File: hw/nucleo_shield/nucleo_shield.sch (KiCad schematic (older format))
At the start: 13 parts, among them CN101 Nucleo-F411RE-CN10, CN71 Nucleo-F411RE-CN7, P12 CONN_RS485_OUT, P13 CONN_RS485_IN, P4 POWER_CON, P6 ETH_CONN, P7 SD_CONN, P8 LCD_CONN, P9 CONN_SCT

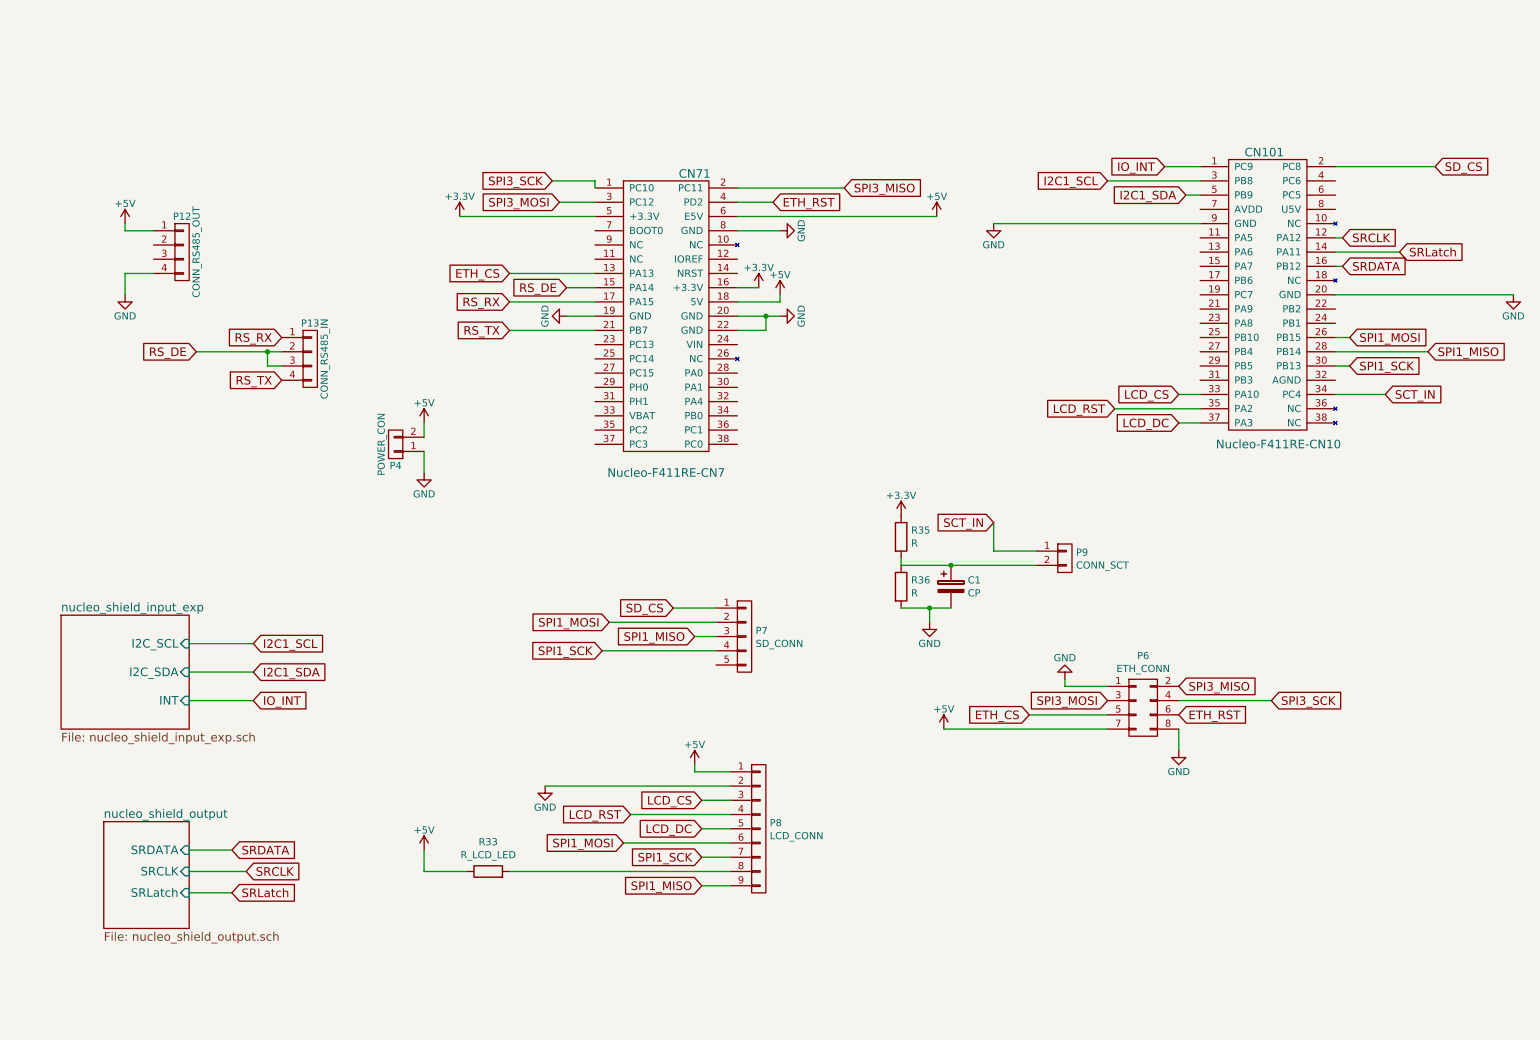
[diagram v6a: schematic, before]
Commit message: Nucleo: add jumpers and outputs
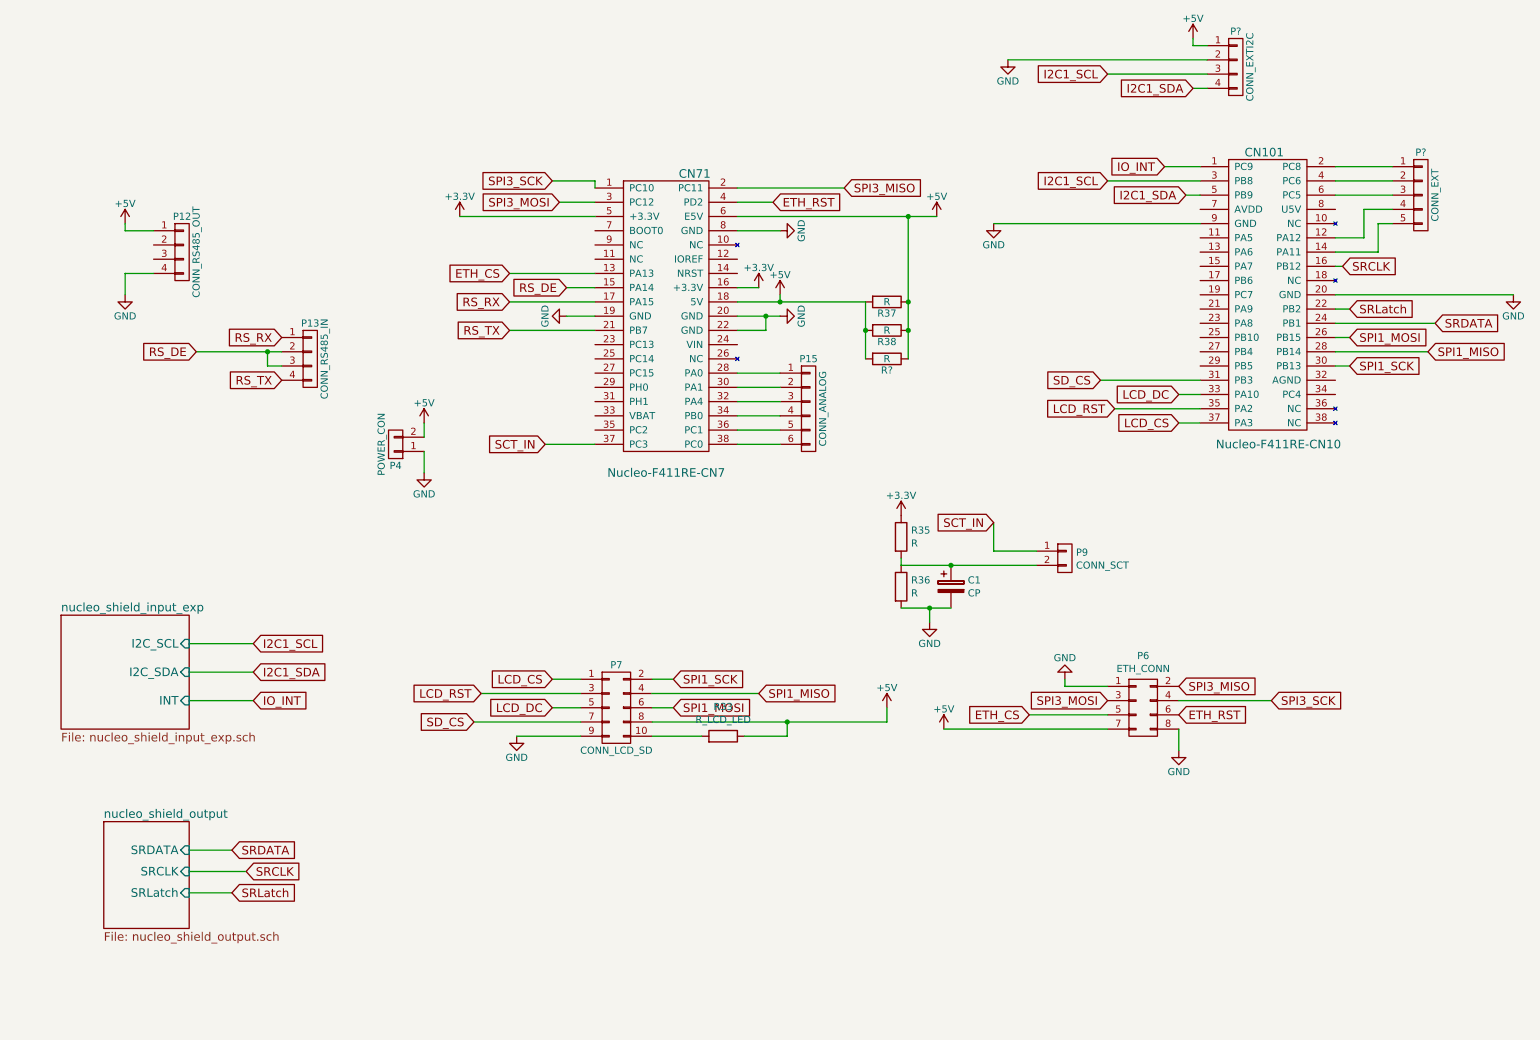
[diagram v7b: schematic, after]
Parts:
- removed P7: SD_CONN, Pin_Headers:Pin_Header_Straight_1x05, symbol CONN_01X05
- removed P8: LCD_CONN, Pin_Headers:Pin_Header_Straight_1x09, symbol CONN_01X09
- added P15: CONN_ANALOG, Pin_Headers:Pin_Header_Straight_1x06, symbol CONN_01X06
- added P7: CONN_LCD_SD, Pin_Headers:Pin_Header_Straight_2x05, symbol CONN_02X05
- added P?: CONN_EXT, symbol CONN_01X05
- added P?: CONN_EXTI2C, symbol CONN_01X04
- added R37, R38, R?: R, Resistors_ThroughHole:Resistor_Horizontal_RM10mm, symbol R
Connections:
- net +5V: now also P7.8 (P8), P?.1 (P1), R37.1, R37.2, R38.1, R38.2, R?.1, R?.2
- net GND: now also P7.9 (P9), P?.2 (P2)
- net I2C1_SCL: now also P?.3 (P3)
- net I2C1_SDA: now also P?.4 (P4)
- net LCD_CS: now also CN101.37 (PA3), P7.1 (P1); no longer CN101.33 (PA10)
- net LCD_DC: now also CN101.33 (PA10), P7.5 (P5); no longer CN101.37 (PA3)
- net LCD_RST: now also P7.3 (P3)
- net SCT_IN: now also CN71.37 (PC3); no longer CN101.34 (PC4)
- net SD_CS: now also CN101.31 (PB3), P7.7 (P7); no longer CN101.2 (PC8)
- net SPI1_MISO: now also P7.4 (P4)
- net SPI1_MOSI: now also P7.6 (P6)
- net SPI1_SCK: now also P7.2 (P2)
- net SRCLK: now also CN101.16 (PB12); no longer CN101.12 (PA12)
- net SRDATA: now also CN101.24 (PB1); no longer CN101.16 (PB12)
- net SRLatch: now also CN101.22 (PB2); no longer CN101.14 (PA11)
- net at CN101.4 (PC6): now also P?.2 (P2)
- net at CN101.6 (PC5): now also P?.3 (P3)
- net at CN71.28 (PA0): now also P15.1 (P1)
- net at CN71.30 (PA1): now also P15.2 (P2)
- net at CN71.32 (PA4): now also P15.3 (P3)
- net at CN71.34 (PB0): now also P15.4 (P4)
- net at CN71.36 (PC1): now also P15.5 (P5)
- net at CN71.38 (PC0): now also P15.6 (P6)
- net at R33.2: now also P7.10 (P10)
- new net: CN101.12 (PA12), P?.4 (P4)
- new net: CN101.14 (PA11), P?.5 (P5)
- new net: CN101.2 (PC8), P?.1 (P1)
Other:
- moved on the sheet: R33

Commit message: Add one wire, expander, etc
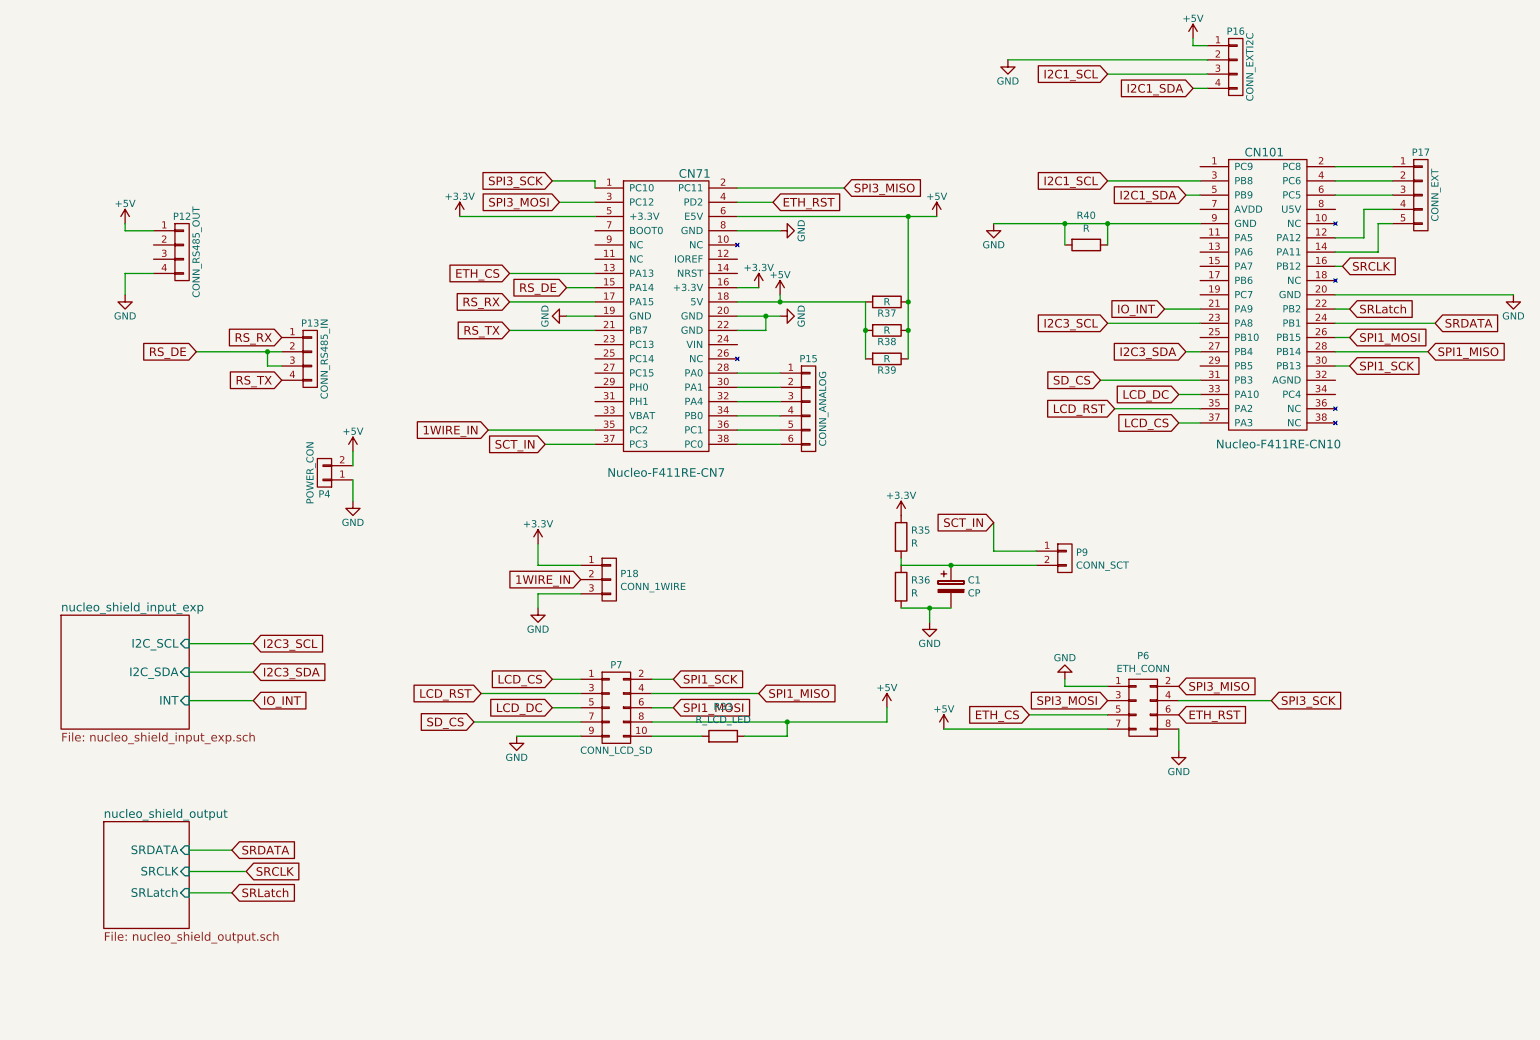
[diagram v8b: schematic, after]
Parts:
- removed R?: R, Resistors_ThroughHole:Resistor_Horizontal_RM10mm, symbol R
- added P18: CONN_1WIRE, Pin_Headers:Pin_Header_Straight_1x03, symbol CONN_01X03
- added R39: R, Resistors_ThroughHole:Resistor_Horizontal_RM20mm, symbol R
- added R40: R, Resistors_ThroughHole:Resistor_Horizontal_RM10mm, symbol R
- P16: renamed from P?; footprint (none) -> Pin_Headers:Pin_Header_Straight_1x04
- P17: renamed from P?; footprint (none) -> Pin_Headers:Pin_Header_Straight_1x05
- R35, R36: footprint Resistors_SMD:R_0805_HandSoldering -> Resistors_ThroughHole:Resistor_Horizontal_RM10mm
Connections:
- net +3V3: now also P18.1 (P1)
- net +5V: now also R39.1, R39.2
- net GND: now also P18.3 (P3), R40.1, R40.2
- net IO_INT: now also CN101.21 (PA9); no longer CN101.1 (PC9)
- net I2C3_SCL: now reaches CN101.23 (PA8)
- net I2C3_SDA: now reaches CN101.27 (PB4)
- net 1WIRE_IN: now reaches CN71.35 (PC2)
- net 1WIRE_IN: now also P18.2 (P2)
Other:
- moved on the sheet: P4
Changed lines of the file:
@@
 LIBS:memory
 LIBS:xilinx
-LIBS:special
 LIBS:microcontrollers
 LIBS:dsp
@@
 L CONN_01X02 P4
 U 1 1 56AB61A1
-P 3300 3600
-F 0 "P4" H 3300 3750 50  0000 C CNN
-F 1 "POWER_CON" V 3400 3600 50  0000 C CNN
-F 2 "w_conn_screw:mors_2p" H 3300 3600 60  0001 C CNN
-F 3 "" H 3300 3600 60  0000 C CNN
-	1    3300 3600
+P 2800 3800
+F 0 "P4" H 2800 3950 50  0000 C CNN
+F 1 "POWER_CON" V 2900 3800 50  0000 C CNN
+F 2 "w_conn_screw:mors_2p" H 2800 3800 60  0001 C CNN
+F 3 "" H 2800 3800 60  0000 C CNN
+	1    2800 3800
 	-1   0    0    1
 $EndComp
@@
 L +5V #PWR09
 U 1 1 56AB6530
-P 3500 3450
-F 0 "#PWR09" H 3500 3300 50  0001 C CNN
-F 1 "+5V" H 3500 3590 50  0000 C CNN
-F 2 "" H 3500 3450 60  0000 C CNN
-F 3 "" H 3500 3450 60  0000 C CNN
-	1    3500 3450
+P 3000 3650
+F 0 "#PWR09" H 3000 3500 50  0001 C CNN
+F 1 "+5V" H 3000 3790 50  0000 C CNN
+F 2 "" H 3000 3650 60  0000 C CNN
+F 3 "" H 3000 3650 60  0000 C CNN
+	1    3000 3650
 	1    0    0    -1
 $EndComp
@@
 L GND #PWR010
 U 1 1 56AB6589
-P 3500 3800
-F 0 "#PWR010" H 3500 3550 50  0001 C CNN
-F 1 "GND" H 3500 3650 50  0000 C CNN
-F 2 "" H 3500 3800 60  0000 C CNN
-F 3 "" H 3500 3800 60  0000 C CNN
-	1    3500 3800
+P 3000 4000
+F 0 "#PWR010" H 3000 3750 50  0001 C CNN
+F 1 "GND" H 3000 3850 50  0000 C CNN
+F 2 "" H 3000 4000 60  0000 C CNN
+F 3 "" H 3000 4000 60  0000 C CNN
+	1    3000 4000
 	1    0    0    -1
 $EndComp
@@
 Text GLabel 2150 6450 2    60   Input ~ 0
 SRDATA
-Text GLabel 8300 1750 0    60   Input ~ 0
-I2C1_SCL
-Text GLabel 8850 1850 0    60   Input ~ 0
-I2C1_SDA
+Text GLabel 8300 2750 0    60   Input ~ 0
+I2C3_SCL
+Text GLabel 8850 2950 0    60   Input ~ 0
+I2C3_SDA
 Text GLabel 6450 1800 2    60   Input ~ 0
 SPI3_MISO
@@
 Text GLabel 4400 1750 0    60   Input ~ 0
 SPI3_SCK
-Text GLabel 8700 1650 0    60   Input ~ 0
+Text GLabel 8700 2650 0    60   Input ~ 0
 IO_INT
 $Sheet
@@
 IO_INT
 Text GLabel 2300 5000 2    60   Input ~ 0
-I2C1_SCL
+I2C3_SCL
 Text GLabel 2300 5200 2    60   Input ~ 0
-I2C1_SDA
+I2C3_SDA
 $Comp
 L CONN_02X04 P6
@@
 F 0 "R35" H 6920 4296 50  0000 L CNN
 F 1 "R" H 6920 4205 50  0000 L CNN
-F 2 "Resistors_SMD:R_0805_HandSoldering" V 6780 4250 50  0001 C CNN
+F 2 "Resistors_ThroughHole:Resistor_Horizontal_RM10mm" V 6780 4250 50  0001 C CNN
 F 3 "" H 6850 4250 50  0000 C CNN
 	1    6850 4250
@@
 F 0 "R36" H 6920 4646 50  0000 L CNN
 F 1 "R" H 6920 4555 50  0000 L CNN
-F 2 "Resistors_SMD:R_0805_HandSoldering" V 6780 4600 50  0001 C CNN
+F 2 "Resistors_ThroughHole:Resistor_Horizontal_RM10mm" V 6780 4600 50  0001 C CNN
 F 3 "" H 6850 4600 50  0000 C CNN
 	1    6850 4600
@@
 	9900 2750 10600 2750
 Wire Wire Line
-	3500 3550 3500 3450
-Wire Wire Line
-	3500 3650 3500 3800
+	3000 3750 3000 3650
+Wire Wire Line
+	3000 3850 3000 4000
 Wire Wire Line
 	3750 2000 4700 2000
@@
 	1850 6750 2150 6750
 Wire Wire Line
-	8300 1750 8950 1750
+	8300 2750 8950 2750
 Wire Wire Line
 	6450 1800 5700 1800
@@
 	4700 1900 4450 1900
 Wire Wire Line
-	8700 1650 8950 1650
-Wire Wire Line
-	8950 1850 8850 1850
+	8700 2650 8950 2650
+Wire Wire Line
+	8950 2950 8850 2950
 Wire Wire Line
 	1850 5000 2300 5000
@@
 $EndComp
 Connection ~ 6000 2600
-Wire Wire Line
-	6900 2000 6900 3000
 Connection ~ 6900 2000
 $Comp
@@
 	0    1    1    0
 $EndComp
-Wire Wire Line
-	6600 2600 6600 3000
-Connection ~ 6900 2600
-$Comp
-L CONN_01X05 P?
+$Comp
+L CONN_01X05 P17
 U 1 1 5733734C
 P 10500 1850
-F 0 "P?" H 10500 2150 50  0000 C CNN
+F 0 "P17" H 10500 2150 50  0000 C CNN
 F 1 "CONN_EXT" V 10600 1850 50  0000 C CNN
-F 2 "" H 10500 1850 60  0000 C CNN
+F 2 "Pin_Headers:Pin_Header_Straight_1x05" H 10500 1850 60  0001 C CNN
 F 3 "" H 10500 1850 60  0000 C CNN
 	1    10500 1850
@@
 	10200 2050 10300 2050
 $Comp
-L R R?
-U 1 1 57337A72
-P 6750 3000
-F 0 "R?" V 6830 3000 50  0000 C CNN
-F 1 "R" V 6750 3000 50  0000 C CNN
-F 2 "Resistors_ThroughHole:Resistor_Horizontal_RM10mm" V 6680 3000 30  0001 C CNN
-F 3 "" H 6750 3000 30  0000 C CNN
-	1    6750 3000
-	0    1    1    0
-$EndComp
-Connection ~ 6600 2800
-Connection ~ 6900 2800
-$Comp
-L CONN_01X04 P?
+L CONN_01X04 P16
 U 1 1 57337E5A
 P 9200 950
-F 0 "P?" H 9200 1200 50  0000 C CNN
+F 0 "P16" H 9200 1200 50  0000 C CNN
 F 1 "CONN_EXTI2C" V 9300 950 50  0000 C CNN
-F 2 "" H 9200 950 60  0000 C CNN
+F 2 "Pin_Headers:Pin_Header_Straight_1x04" H 9200 950 60  0001 C CNN
 F 3 "" H 9200 950 60  0000 C CNN
 	1    9200 950
@@
 	9000 1000 8300 1000
 $Comp
-L GND #PWR?
+L GND #PWR021
 U 1 1 573383E2
 P 7600 900
-F 0 "#PWR?" H 7600 650 50  0001 C CNN
+F 0 "#PWR021" H 7600 650 50  0001 C CNN
 F 1 "GND" H 7600 750 50  0000 C CNN
 F 2 "" H 7600 900 60  0000 C CNN
@@
 	9000 900  7600 900
 $Comp
-L +5V #PWR?
+L +5V #PWR022
 U 1 1 573384B1
 P 8900 750
-F 0 "#PWR?" H 8900 600 50  0001 C CNN
+F 0 "#PWR022" H 8900 600 50  0001 C CNN
 F 1 "+5V" H 8900 890 50  0000 C CNN
 F 2 "" H 8900 750 60  0000 C CNN
@@
 Wire Wire Line
 	8900 800  9000 800
+Text GLabel 8850 1850 0    60   Input ~ 0
+I2C1_SDA
+Text GLabel 8300 1750 0    60   Input ~ 0
+I2C1_SCL
+Wire Wire Line
+	8300 1750 8950 1750
+Wire Wire Line
+	8850 1850 8950 1850
+$Comp
+L R R40
+U 1 1 5733E4B6
+P 8150 2200
+F 0 "R40" V 7943 2200 50  0000 C CNN
+F 1 "R" V 8034 2200 50  0000 C CNN
+F 2 "Resistors_ThroughHole:Resistor_Horizontal_RM10mm" V 8080 2200 50  0001 C CNN
+F 3 "" H 8150 2200 50  0000 C CNN
+	1    8150 2200
+	0    1    1    0
+$EndComp
+Wire Wire Line
+	8000 2200 8000 2050
+Connection ~ 8000 2050
+Wire Wire Line
+	8300 2200 8300 2050
+Connection ~ 8300 2050
+Wire Wire Line
+	6900 2000 6900 3000
+Wire Wire Line
+	6600 2600 6600 3000
+Connection ~ 6900 2600
+Text GLabel 3950 3500 0    60   Input ~ 0
+1WIRE_IN
+Wire Wire Line
+	3950 3500 4700 3500
+$Comp
+L CONN_01X03 P18
+U 1 1 5733A232
+P 4800 4550
+F 0 "P18" H 4878 4591 50  0000 L CNN
+F 1 "CONN_1WIRE" H 4878 4500 50  0000 L CNN
+F 2 "Pin_Headers:Pin_Header_Straight_1x03" H 4800 4550 50  0001 C CNN
+F 3 "" H 4800 4550 50  0000 C CNN
+	1    4800 4550
+	1    0    0    -1
+$EndComp
+Text GLabel 4600 4550 0    60   Input ~ 0
+1WIRE_IN
+$Comp
+L +3.3V #PWR023
+U 1 1 5733BF71
+P 4300 4300
+F 0 "#PWR023" H 4300 4150 50  0001 C CNN
+F 1 "+3.3V" H 4300 4440 50  0000 C CNN
+F 2 "" H 4300 4300 60  0000 C CNN
+F 3 "" H 4300 4300 60  0000 C CNN
+	1    4300 4300
+	1    0    0    -1
+$EndComp
+$Comp
+L GND #PWR024
+U 1 1 5733BFD9
+P 4300 4750
+F 0 "#PWR024" H 4300 4500 50  0001 C CNN
+F 1 "GND" H 4300 4600 50  0000 C CNN
+F 2 "" H 4300 4750 60  0000 C CNN
+F 3 "" H 4300 4750 60  0000 C CNN
+	1    4300 4750
+	1    0    0    -1
+$EndComp
+Wire Wire Line
+	4300 4300 4300 4450
+Wire Wire Line
+	4300 4450 4600 4450
+Wire Wire Line
+	4600 4650 4300 4650
+Wire Wire Line
+	4300 4650 4300 4750
+$Comp
+L R R39
+U 1 1 5733CEEB
+P 6750 3000
+F 0 "R39" V 6830 3000 50  0000 C CNN
+F 1 "R" V 6750 3000 50  0000 C CNN
+F 2 "Resistors_ThroughHole:Resistor_Horizontal_RM20mm" V 6680 3000 30  0001 C CNN
+F 3 "" H 6750 3000 30  0000 C CNN
+	1    6750 3000
+	0    1    1    0
+$EndComp
+Connection ~ 6600 2800
+Connection ~ 6900 2800
 $EndSCHEMATC
